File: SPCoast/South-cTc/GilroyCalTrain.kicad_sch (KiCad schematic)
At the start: 1 part

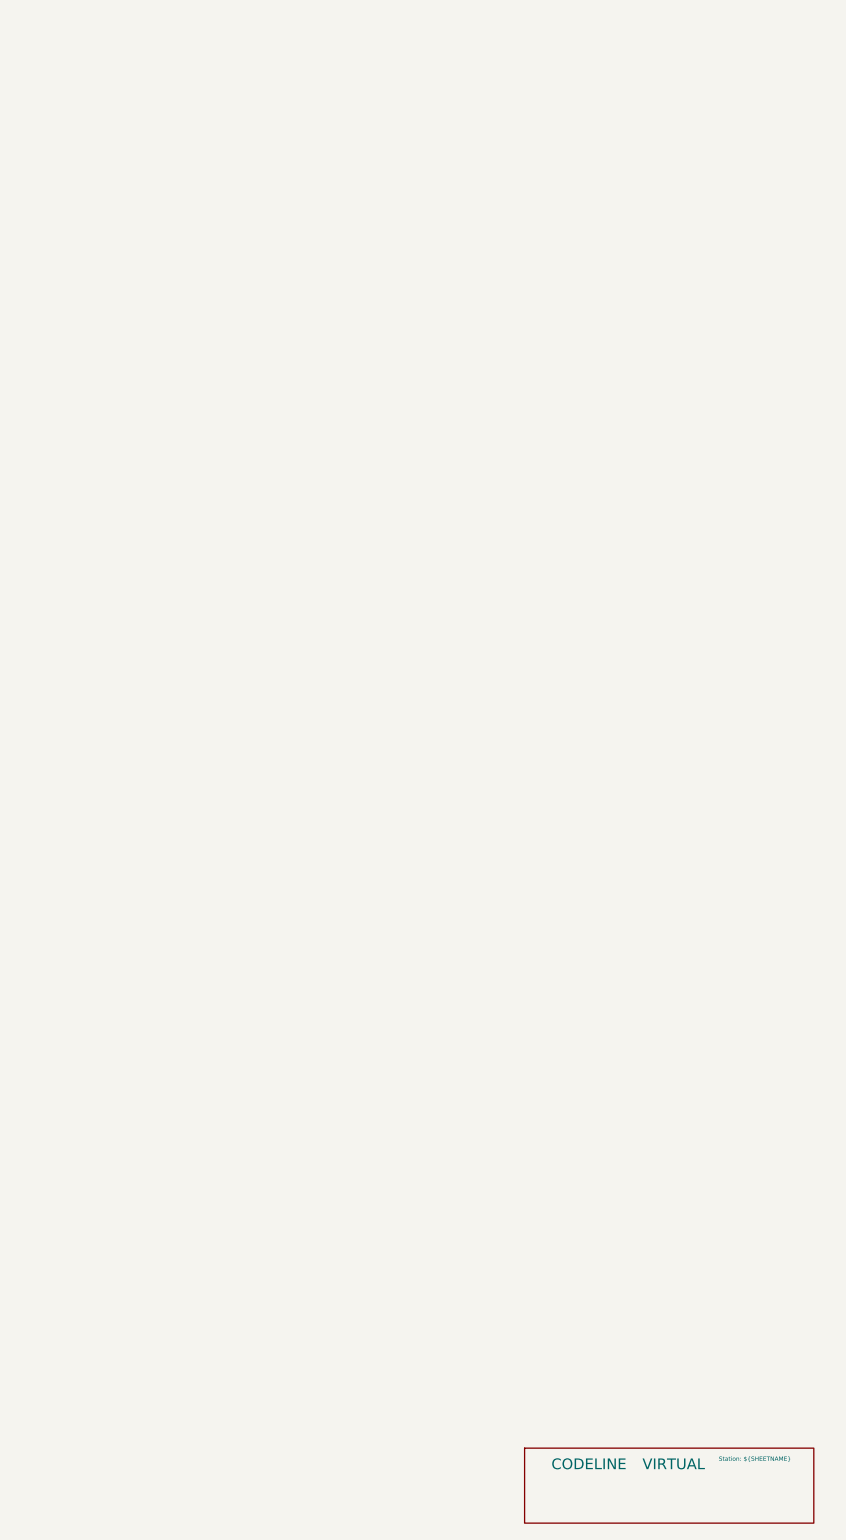
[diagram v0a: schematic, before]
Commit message: SPCoast: derail pin R, track circuit names end in T, code line symbols on the root sheet
Working-tree changes from the 2026-10-01..03 vocabulary review with
FieldUnit-Subdivision (docs/adr/0001-code-line-type-contract.md):

- Switch_Powered_Derail pin 2 is R (through path = REVERSE) in the seven
  plant schematics (library Railroad.kicad_sym renamed alongside; not in git)
- Luchessa track circuits renamed to end in T (1SAT, 2NAAT, ...); MC1 moved
  to CP Gilroy's house
- South-cTc: transports (MQTT, TimeCode, CMRInet, Loconet) on the root
  sheet on the CtcMachine Transports pin; field stations as encoding
  instances on the Luchessa sheet; two Luchessa lamp tokens renamed
- Six plant projects (Christopher, Corporal, GilroyCalTrain,
  GilroyInterchange, Sargent, Watsonville) added as drawn so far; Watsonville
  updated 2026-10-02

Co-Authored-By: Claude Fable 5.1 <noreply@anthropic.com>
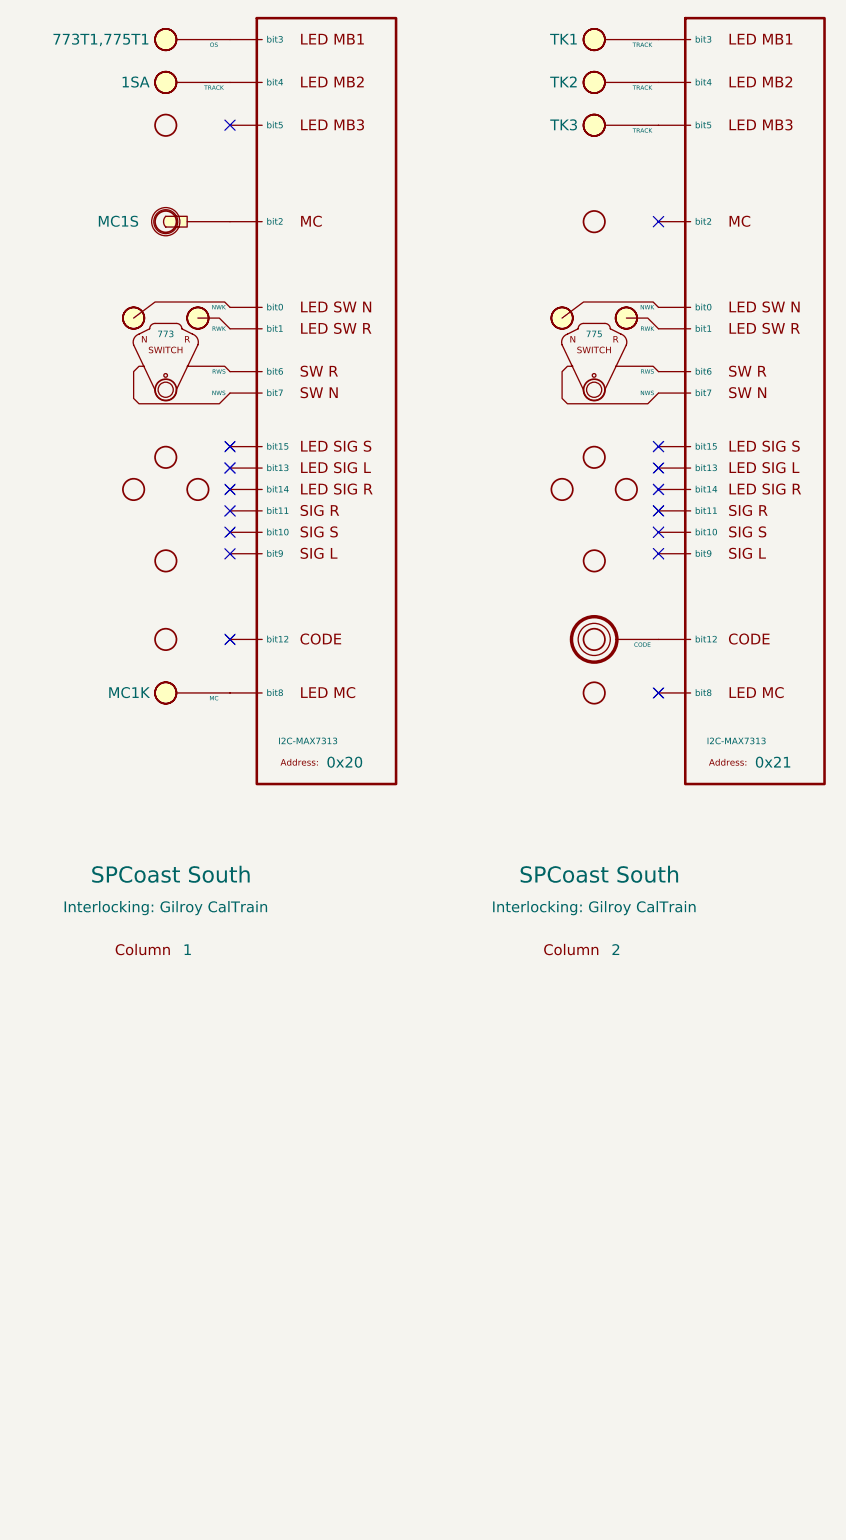
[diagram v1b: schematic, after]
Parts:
- removed CODELINE1: VIRTUAL, symbol RailroadPanel:Codeline-Virtual
- added CDE2: CODE, symbol RailroadPanel:PanelCode
- added COL21: 1, symbol RailroadPanel:PanelColumn
- added COL22: 2, symbol RailroadPanel:PanelColumn
- added LMP11: OS, symbol RailroadPanel:PanelLamp-RED
- added LMP12, LMP21, LMP22, LMP23: TRACK, symbol RailroadPanel:PanelLamp-YELLOW
- added MCK1: MC, symbol RailroadPanel:PanelLamp-YELLOW
- added MCL1: MC1, symbol RailroadPanel:PanelMCall
- added SWL1: 773, symbol RailroadPanel:PanelSwitch
- added SWL2: 775, symbol RailroadPanel:PanelSwitch
- added U21: 0x20, symbol RailroadPanel:PanelColumn-MAX7313
- added U22: 0x21, symbol RailroadPanel:PanelColumn-MAX7313
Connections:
- new net: COL21.1 (Column), LMP11.1 (Column)
- new net: LMP11.2 (LAMP), U21.4 (bit3)
- new net: COL22.5 (Column), SWL2.1 (Column)
- new net: SWL2.2 (NWS), U22.8 (bit7)
- new net: SWL2.3 (RWS), U22.7 (bit6)
- new net: SWL2.4 (RWK), U22.2 (bit1)
- new net: SWL2.5 (NWK), U22.1 (bit0)
- new net: COL21.2 (Column), LMP12.1 (Column)
- new net: COL21.4 (Column), MCL1.1 (Column)
- new net: COL21.5 (Column), SWL1.1 (Column)
- new net: COL21.8 (Column), MCK1.1 (Column)
- new net: CDE2.1 (Column), COL22.7 (Column)
- new net: CDE2.2 (CODE), U22.13 (bit12)
- new net: SWL1.2 (NWS), U21.8 (bit7)
- new net: SWL1.3 (RWS), U21.7 (bit6)
- new net: SWL1.4 (RWK), U21.2 (bit1)
- new net: SWL1.5 (NWK), U21.1 (bit0)
- new net: COL22.1 (Column), LMP21.1 (Column)
- new net: LMP21.2 (LAMP), U22.4 (bit3)
- new net: MCL1.2 (SW), U21.3 (bit2)
- new net: LMP12.2 (LAMP), U21.5 (bit4)
- new net: MCK1.2 (LAMP), U21.9 (bit8)
- new net: COL22.2 (Column), LMP22.1 (Column)
- new net: LMP22.2 (LAMP), U22.5 (bit4)
- new net: LMP23.2 (LAMP), U22.6 (bit5)
- new net: COL22.3 (Column), LMP23.1 (Column)
- no-connect marks 0 -> 16

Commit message: SPCoast: Address field and Kind on PanelColumn-MAX7313; encoding Values; HBA; Watsonville update
Owner's drawing changes of 2026-10-02..03 (FieldUnit-Subdivision ADR 0002 D18
and the owner's responses):

- PanelColumn-MAX7313: the expander address moves from the Value to an
  Address field (Value is ${Address}); BusKind renamed Kind (I2C-MAX7313)
- Luchessa encoding symbols: Value "US&S 506 time-coded DC pulses"
- Sargent: HBD renamed HBA; traffic indications [NSEW]FLK
- Watsonville schematic brought to a usable state
- Luchessa plant: track circuits end in T; MC1 at CP Gilroy's house

Co-Authored-By: Claude Fable 5.1 <noreply@anthropic.com>
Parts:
- U21: value 0x20 -> ${ADDRESS}; Address (none) -> 0x20; BusKind I2C-MAX7313 -> (none); Kind (none) -> I2C-MAX7313
- U22: value 0x21 -> ${ADDRESS}; Address (none) -> 0x21; BusKind I2C-MAX7313 -> (none); Kind (none) -> I2C-MAX7313
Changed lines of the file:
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@@
 			)
 		)
-		(property "Value" "0x20"
-			(at 99.06 112.395 0)
+		(property "Value" "${ADDRESS}"
+			(at 102.362 111.76 0)
+			(hide yes)
 			(show_name no)
 			(do_not_autoplace yes)
@@
 			)
 		)
-		(property "BusKind" "I2C-MAX7313"
+		(property "Role" "IODRIVER"
+			(at 97.79 107.315 0)
+			(hide yes)
+			(show_name no)
+			(do_not_autoplace no)
+			(effects
+				(font
+					(size 1.27 1.27)
+				)
+			)
+		)
+		(property "Kind" "I2C-MAX7313"
 			(at 93.345 109.855 0)
 			(show_name no)
@@
 			)
 		)
-		(property "Role" "IODRIVER"
-			(at 99.06 72.39 0)
-			(hide yes)
+		(property "Address" "0x20"
+			(at 100.6281 112.3109 0)
 			(show_name no)
 			(do_not_autoplace no)
@@
 			)
 		)
-		(property "Value" "0x21"
+		(property "Value" "${ADDRESS}"
 			(at 149.86 112.395 0)
+			(hide yes)
 			(show_name no)
 			(do_not_autoplace yes)
@@
 			)
 		)
-		(property "BusKind" "I2C-MAX7313"
+		(property "Role" "IODRIVER"
+			(at 148.59 107.315 0)
+			(hide yes)
+			(show_name no)
+			(do_not_autoplace no)
+			(effects
+				(font
+					(size 1.27 1.27)
+				)
+			)
+		)
+		(property "Kind" "I2C-MAX7313"
 			(at 144.145 109.855 0)
 			(show_name no)
-			(do_not_autoplace yes)
+			(do_not_autoplace no)
 			(effects
 				(font
@@
 			)
 		)
-		(property "Role" "IODRIVER"
-			(at 149.86 72.39 0)
-			(hide yes)
-			(show_name no)
-			(do_not_autoplace no)
+		(property "Address" "0x21"
+			(at 152.146 112.522 0)
+			(show_name no)
+			(do_not_autoplace no)

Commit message: fix(kicad): approach circuits end in T; desk tokens follow
Plants: Christopher 1NA/2NA/1SA/2SA, GilroyCalTrain 1NA/1SA, GilroyInterchange
1SA, Sargent 1NA/1SA/2SA gain the final T (ADR 0003 D4). Sargent's reference
Corporal:2NA becomes Corporal:2NAT, the circuit Corporal draws.

Desk (South-cTc sheets): IndicationToken follows the plants for Christopher,
GilroyCalTrain, GilroyInterchange; Corporal 1SA becomes 1SAT (the plant already
had it); Christopher 815T2 becomes 815AT1 (the OS circuit of switch 815A).

Not changed, awaiting decisions in the dry-run report: 0<n>T renames (IND,
TK<n>, Interchange, 2NAAT, 2SAT), section 2 of an approach, unnamed circuits,
Watsonville, CP_Watsonville: references, 1TK.

Verified: netlists rebuilt for all affected projects; of 33 desk circuit tokens,
5 now match no plant circuit (was 11): 1TK, CP_Watsonville:SA1,
CP_Watsonville:837T1, Watsonville 1NAK and 2NAK. KiCad closed, no ~*.lck.

Co-Authored-By: Claude Sonnet 5.5 <noreply@anthropic.com>
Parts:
- LMP12: IndicationToken 1SA -> 1SAT
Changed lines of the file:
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@@
 			)
 		)
-		(property "IndicationToken" "1SA"
+		(property "IndicationToken" "1SAT"
 			(at 78.105 31.75 0)
 			(show_name no)

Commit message: fix(kicad): GilroyCalTrain yard circuits TK1..TK3 become 01T..03T
Each TK circuit shares a net with the Rule 93 yard marker the owner named
Track 1..3, so the zero-prefixed form 0<n>T follows the crew's track numbers.
Desk IndicationToken follows.

Verified: netlist pairs TK1/Track 1, TK2/Track 2, TK3/Track 3; desk col 2
lamps now carry 01T, 02T, 03T.

Co-Authored-By: Claude Sonnet 5.5 <noreply@anthropic.com>
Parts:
- LMP21: IndicationToken TK1 -> 01T
- LMP22: IndicationToken TK2 -> 02T
- LMP23: IndicationToken TK3 -> 03T
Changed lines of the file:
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@@
 			)
 		)
-		(property "IndicationToken" "TK1"
+		(property "IndicationToken" "01T"
 			(at 128.905 26.67 0)
 			(show_name no)
@@
 			)
 		)
-		(property "IndicationToken" "TK2"
+		(property "IndicationToken" "02T"
 			(at 128.905 31.75 0)
 			(show_name no)
@@
 			)
 		)
-		(property "IndicationToken" "TK3"
+		(property "IndicationToken" "03T"
 			(at 128.905 36.83 0)
 			(show_name no)

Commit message: SPCoast: owner's edits: Gilroy names normalized to the spaced form (baseline)
GilroyInterchange title block and the desk GilroyCalTrain column Interlocking values now use the spaced spelling; names without spaces normalize to the same value.

Verified: netlists rebuild; no UUID regression.

Co-Authored-By: Claude Sonnet 5.5 <noreply@anthropic.com>
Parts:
- COL21, COL22: Interlocking Gilroy CalTrain -> Gilroy Caltrain
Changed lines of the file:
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@@
 			)
 		)
-		(property "Interlocking" "Gilroy CalTrain"
+		(property "Interlocking" "Gilroy Caltrain"
 			(at 80.01 129.54 0)
 			(show_name yes)
@@
 			)
 		)
-		(property "Interlocking" "Gilroy CalTrain"
+		(property "Interlocking" "Gilroy Caltrain"
 			(at 130.81 129.54 0)
 			(show_name yes)
